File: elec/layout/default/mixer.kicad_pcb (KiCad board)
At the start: 2 copper layers, 87.5 x 28.2 mm, 9 parts

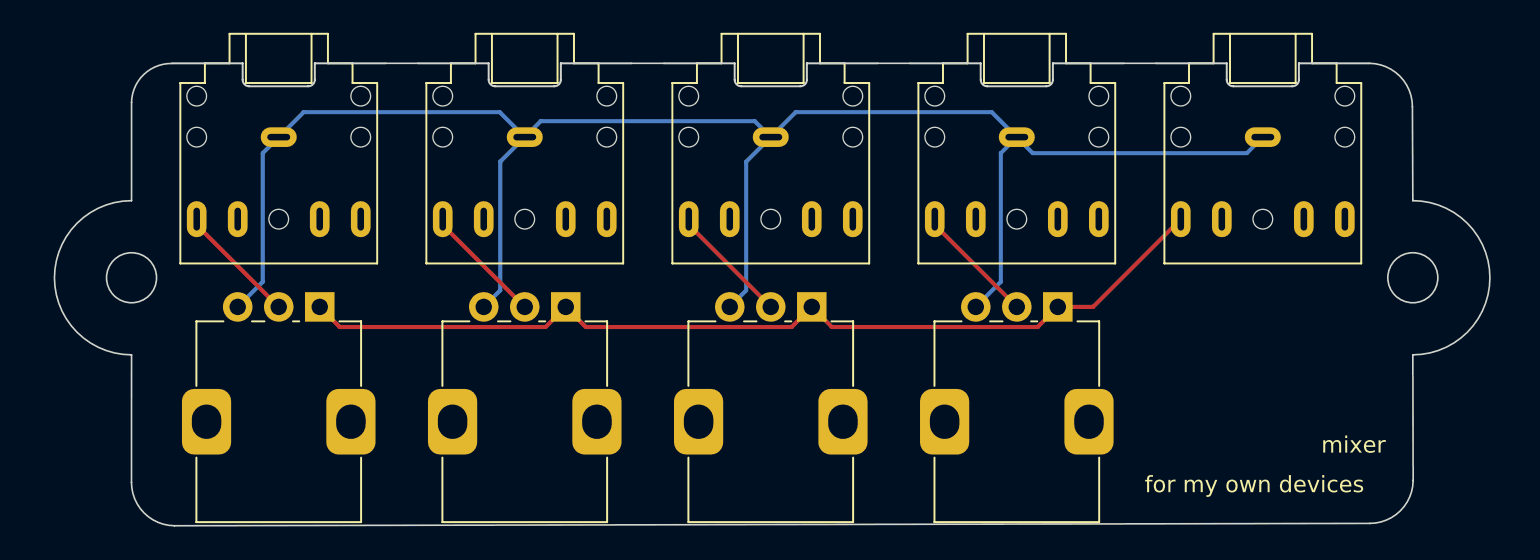
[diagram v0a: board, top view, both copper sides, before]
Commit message: creates switch board
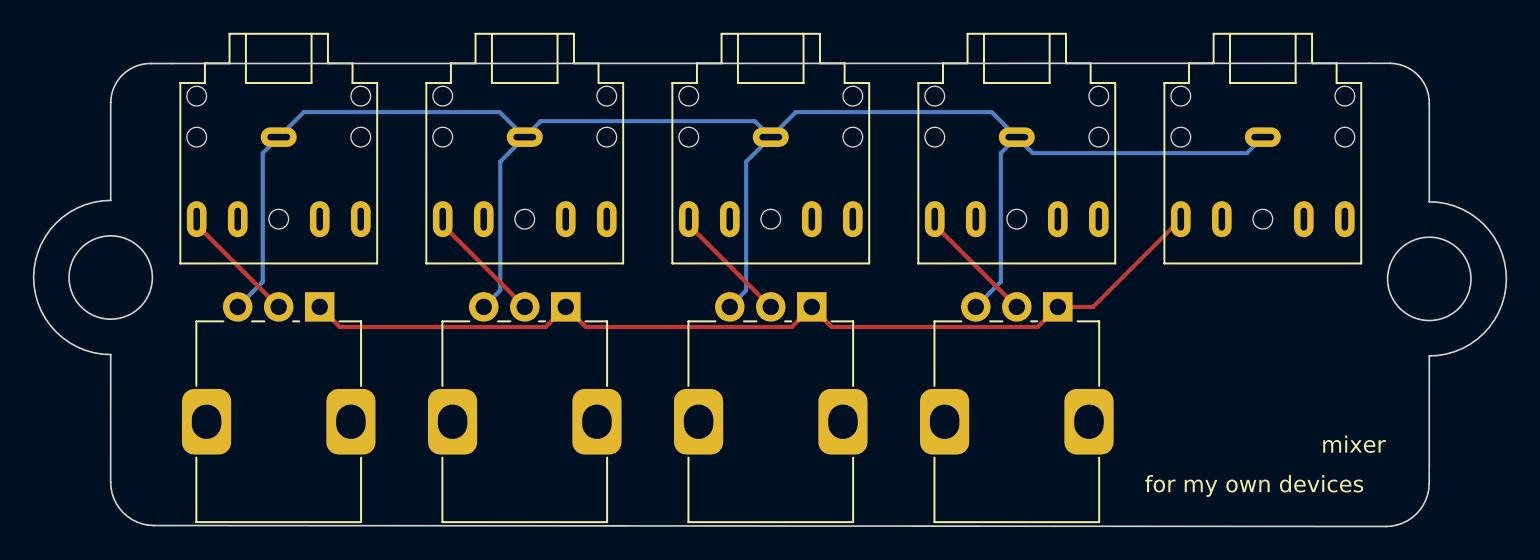
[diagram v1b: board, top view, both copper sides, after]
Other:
- board size 87.5 x 28.2 mm -> 89.8 x 28.2 mm
